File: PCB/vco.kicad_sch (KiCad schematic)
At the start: 16 parts, among them J5 VCO, Q3 2N3904, Q4 2N3904, U1 LM324

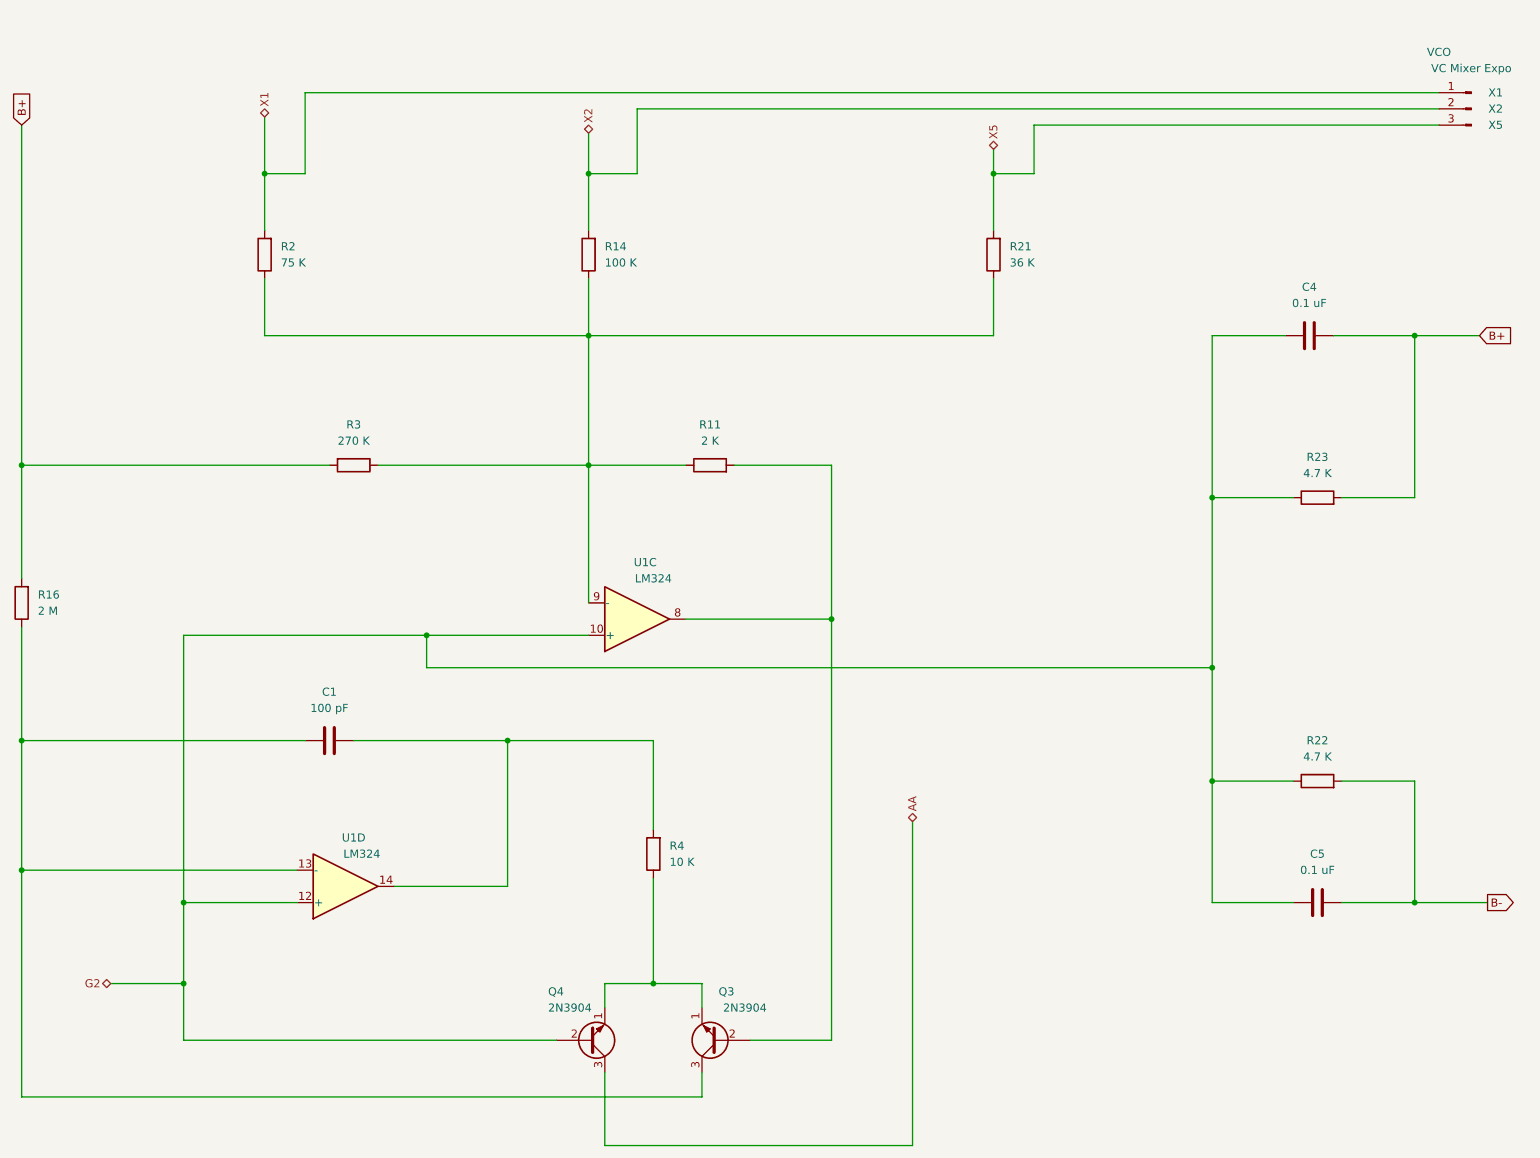
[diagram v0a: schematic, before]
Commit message: Change TO-92 transistors to wide package to avoid shorting during soldering
Added B- hole for speaker
Added more vias to shorten traces
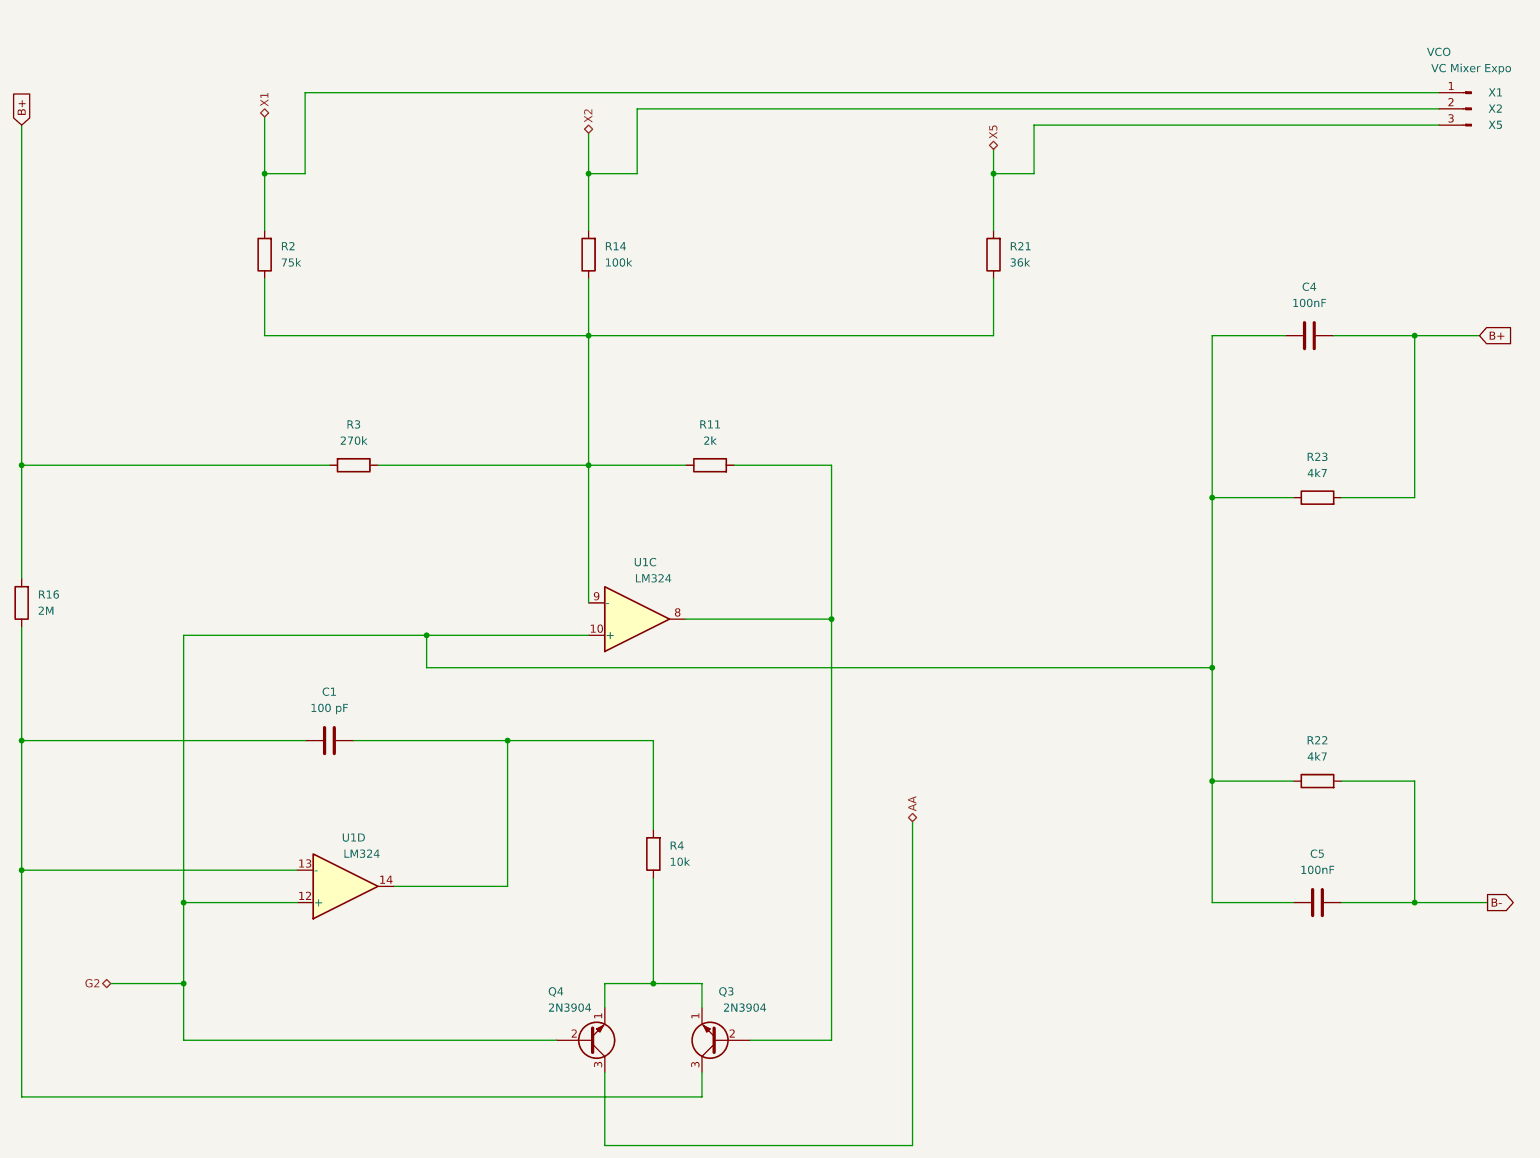
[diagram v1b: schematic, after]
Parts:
- C4, C5: value 0.1 uF -> 100nF
- R11: value 2 K -> 2k
- R14: value 100 K -> 100k
- R16: value 2 M -> 2M
- R2: value 75 K -> 75k
- R21: value 36 K -> 36k
- R22, R23: value 4.7 K -> 4k7
- R3: value 270 K -> 270k
- R4: value 10 K -> 10k
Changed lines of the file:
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@@
 			)
 		)
-		(property "Value" "270 K"
+		(property "Value" "270k"
 			(at 77.47 80.01 90)
 			(show_name no)
@@
 			)
 		)
-		(property "Value" "0.1 uF"
+		(property "Value" "100nF"
 			(at 227.33 58.42 90)
 			(show_name no)
@@
 			)
 		)
-		(property "Value" "4.7 K"
+		(property "Value" "4k7"
 			(at 228.6 85.09 90)
 			(show_name no)
@@
 			)
 		)
-		(property "Value" "2 M"
+		(property "Value" "2M"
 			(at 27.94 106.68 0)
 			(show_name no)
@@
 			)
 		)
-		(property "Value" "75 K"
+		(property "Value" "75k"
 			(at 66.04 52.07 0)
 			(show_name no)
@@
 			)
 		)
-		(property "Value" "0.1 uF"
+		(property "Value" "100nF"
 			(at 228.6 147.32 90)
 			(show_name no)
@@
 			)
 		)
-		(property "Value" "2 K"
+		(property "Value" "2k"
 			(at 133.35 80.01 90)
 			(show_name no)
@@
 			)
 		)
-		(property "Value" "4.7 K"
+		(property "Value" "4k7"
 			(at 228.6 129.54 90)
 			(show_name no)
@@
 			)
 		)
-		(property "Value" "10 K"
+		(property "Value" "10k"
 			(at 127 146.05 0)
 			(show_name no)
@@
 			)
 		)
-		(property "Value" "36 K"
+		(property "Value" "36k"
 			(at 180.34 52.07 0)
 			(show_name no)
@@
 		(fields_autoplaced yes)
 		(property "Reference" "R14"
-			(at 116.84 49.53 0)
+			(at 116.84 49.5299 0)
 			(show_name no)
 			(do_not_autoplace no)
@@
 			)
 		)
-		(property "Value" "100 K"
-			(at 116.84 52.07 0)
-			(show_name no)
-			(do_not_autoplace no)
+		(property "Value" "100k"
+			(at 116.84 52.0699 0)
+			(show_name no)
+			(do_not_autoplace no)

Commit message: Necessary Changes to Schematic and PCB
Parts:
- added CV1: 100k, Resistor_THT:R_Axial_DIN0207_L6.3mm_D2.5mm_P10.16mm_Horizontal, symbol Device:R
- J5: footprint Connector_PinHeader_2.00mm:PinHeader_1x03_P2.00mm_Vertical -> Connector_PinSocket_2.54mm:PinSocket_1x04_P2.54mm_Vertical; symbol Connector:Conn_01x03_Pin -> Connector:Conn_01x04_Pin; CV (none) -> CV
- Q3, Q4: footprint Package_TO_SOT_THT:TO-92_Inline -> Package_TO_SOT_THT:TO-92_Inline_Wide
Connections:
- net at R11.1, R14.1, R2.1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: now also CV1.1
- new net: CV1.2, J5.4 (Pin_4)
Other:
- note added: "C4 and C5 close to U1 LM324 power pins."
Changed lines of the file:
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@@
 		(comment 4 "Created: 2023-06-12")
+	)
+	(text "C4 and C5\nclose to U1 \nLM324 power\npins.\n"
+		(exclude_from_sim no)
+		(at 225.044 113.538 0)
+		(effects
+			(font
+				(size 1.27 1.27)
+			)
+			(justify left bottom)
+		)
 	)
 	(junction
@@
 	)
 	(junction
+		(at 177.8 63.5)
+		(diameter 0)
+		(color 0 0 0 0)
+	)
+	(junction
 		(at 212.09 133.35)
 		(diameter 0)
@@
 	(wire
 		(pts
+			(xy 201.93 54.61) (xy 201.93 63.5)
+		)
+		(stroke
+			(width 0)
+			(type dash)
+		)
+	)
+	(wire
+		(pts
 			(xy 124.46 165.1) (xy 132.08 165.1)
 		)
@@
 	(wire
 		(pts
+			(xy 201.93 63.5) (xy 177.8 63.5)
+		)
+		(stroke
+			(width 0)
+			(type dash)
+		)
+	)
+	(wire
+		(pts
 			(xy 116.84 179.07) (xy 116.84 190.5)
 		)
@@
 	(wire
 		(pts
+			(xy 201.93 33.02) (xy 201.93 46.99)
+		)
+		(stroke
+			(width 0)
+			(type dash)
+		)
+	)
+	(wire
+		(pts
 			(xy 63.5 63.5) (xy 63.5 54.61)
 		)
@@
 			(width 0)
 			(type default)
+		)
+	)
+	(wire
+		(pts
+			(xy 247.65 33.02) (xy 201.93 33.02)
+		)
+		(stroke
+			(width 0)
+			(type dash)
 		)
 	)
@@
 	(symbol
 		(lib_id "Device:R")
+		(at 201.93 50.8 180)
+		(unit 1)
+		(body_style 1)
+		(exclude_from_sim no)
+		(in_bom yes)
+		(on_board yes)
+		(in_pos_files yes)
+		(dnp no)
+		(fields_autoplaced yes)
+		(property "Reference" "CV1"
+			(at 204.47 49.5299 0)
+			(show_name no)
+			(do_not_autoplace no)
+			(effects
+				(font
+					(size 1.27 1.27)
+				)
+				(justify right)
+			)
+		)
+		(property "Value" "100k"
+			(at 204.47 52.0699 0)
+			(show_name no)
+			(do_not_autoplace no)
+			(effects
+				(font
+					(size 1.27 1.27)
+				)
+				(justify right)
+			)
+		)
+		(property "Footprint" "Resistor_THT:R_Axial_DIN0207_L6.3mm_D2.5mm_P10.16mm_Horizontal"
+			(at 203.708 50.8 90)
+			(hide yes)
+			(show_name no)
+			(do_not_autoplace no)
+			(effects
+				(font
+					(size 1.27 1.27)
+				)
+			)
+		)
+		(property "Datasheet" ""
+			(at 201.93 50.8 0)
+			(hide yes)
+			(show_name no)
+			(do_not_autoplace no)
+			(effects
+				(font
+					(size 1.27 1.27)
+				)
+			)
+		)
+		(property "Description" ""
+			(at 201.93 50.8 0)
+			(hide yes)
+			(show_name no)
+			(do_not_autoplace no)
+			(effects
+				(font
+					(size 1.27 1.27)
+				)
+			)
+		)
+		(pin "1"
+		)
+		(pin "2"
+		)
+		(instances
+			(project "Noise Toaster PCB"
+				(path "/7be3f398-d902-4566-9ee4-0bff072cd47e/d0369b76-3398-4137-86ba-22490a5aca99"
+					(reference "CV1")
+					(unit 1)
+				)
+			)
+		)
+	)
+	(symbol
+		(lib_id "Device:R")
 		(at 133.35 83.82 90)
 		(unit 1)
@@
 			)
 		)
-		(property "Footprint" "Package_TO_SOT_THT:TO-92_Inline"
+		(property "Footprint" "Package_TO_SOT_THT:TO-92_Inline_Wide"
 			(at 129.54 172.085 0)
 			(hide yes)
@@
 	)
 	(symbol
-		(lib_id "Connector:Conn_01x03_Pin")
+		(lib_id "Connector:Conn_01x04_Pin")
 		(at 252.73 27.94 0)
 		(mirror y)
@@
 			)
 		)
-		(property "Footprint" "Connector_PinHeader_2.00mm:PinHeader_1x03_P2.00mm_Vertical"
+		(property "Footprint" "Connector_PinSocket_2.54mm:PinSocket_1x04_P2.54mm_Vertical"
 			(at 252.73 27.94 0)
 			(hide yes)
@@
 			)
 		)
-		(property "Description" ""
+		(property "Description" "Generic connector, single row, 01x04, script generated"
 			(at 252.73 27.94 0)
 			(hide yes)
@@
 			)
 		)
+		(property "CV" "CV"
+			(at 256.54 33.02 0)
+			(show_name no)
+			(do_not_autoplace no)
+			(effects
+				(font
+					(size 1.27 1.27)
+				)
+			)
+		)
 		(pin "1"
 		)
@@
 		)
 		(pin "3"
+		)
+		(pin "4"
 		)
 		(instances
@@
 			)
 		)
-		(property "Footprint" "Package_TO_SOT_THT:TO-92_Inline"
+		(property "Footprint" "Package_TO_SOT_THT:TO-92_Inline_Wide"
 			(at 119.38 172.085 0)
 			(hide yes)
